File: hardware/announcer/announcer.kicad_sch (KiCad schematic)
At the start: 5 parts, among them Q1 S8050

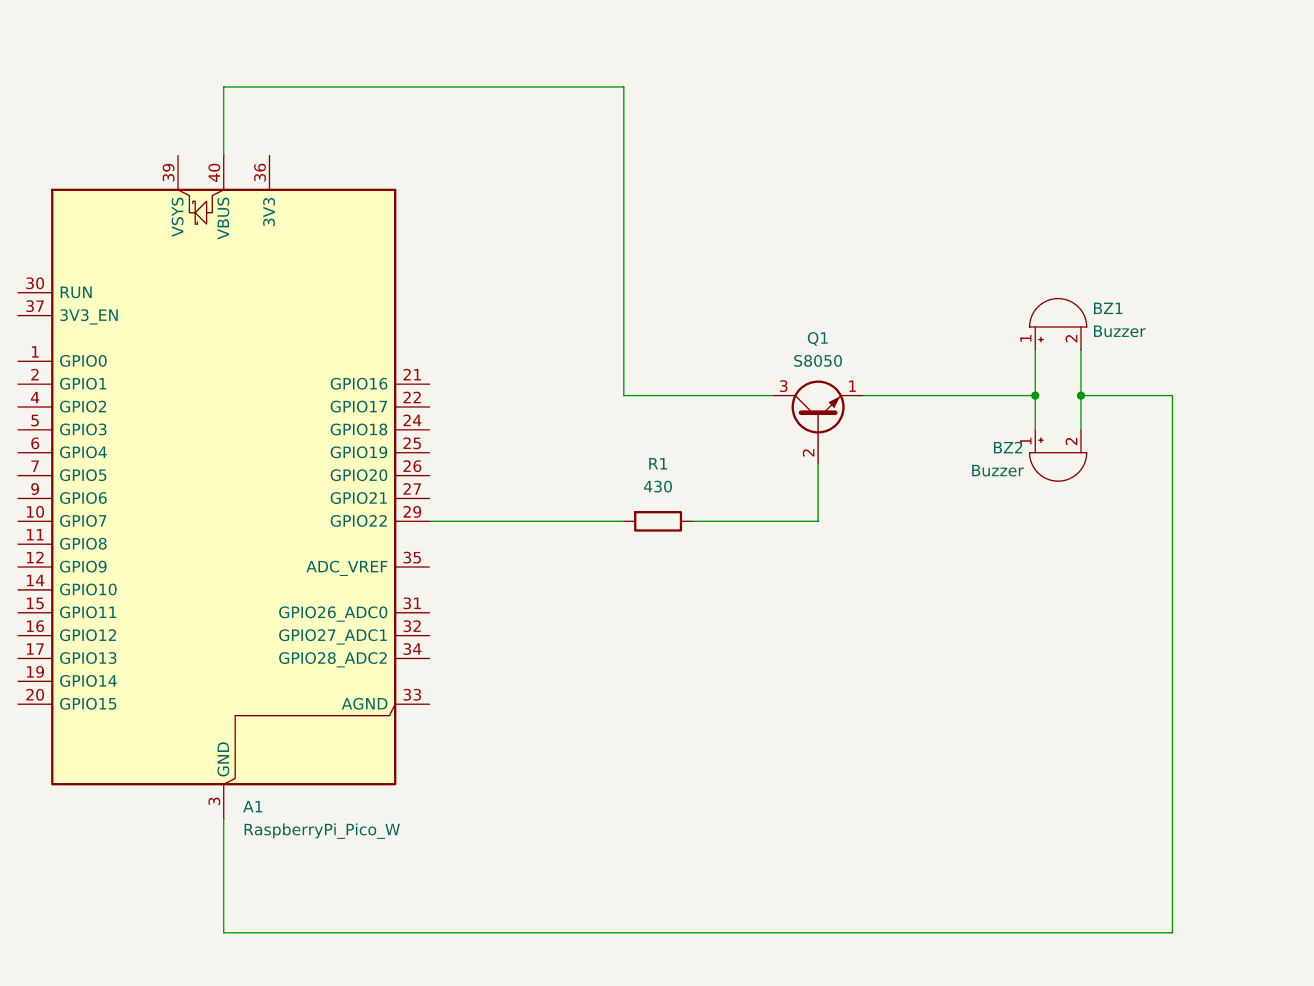
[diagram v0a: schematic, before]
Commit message: hardware announcer: updated schematic to include button and status LEDs
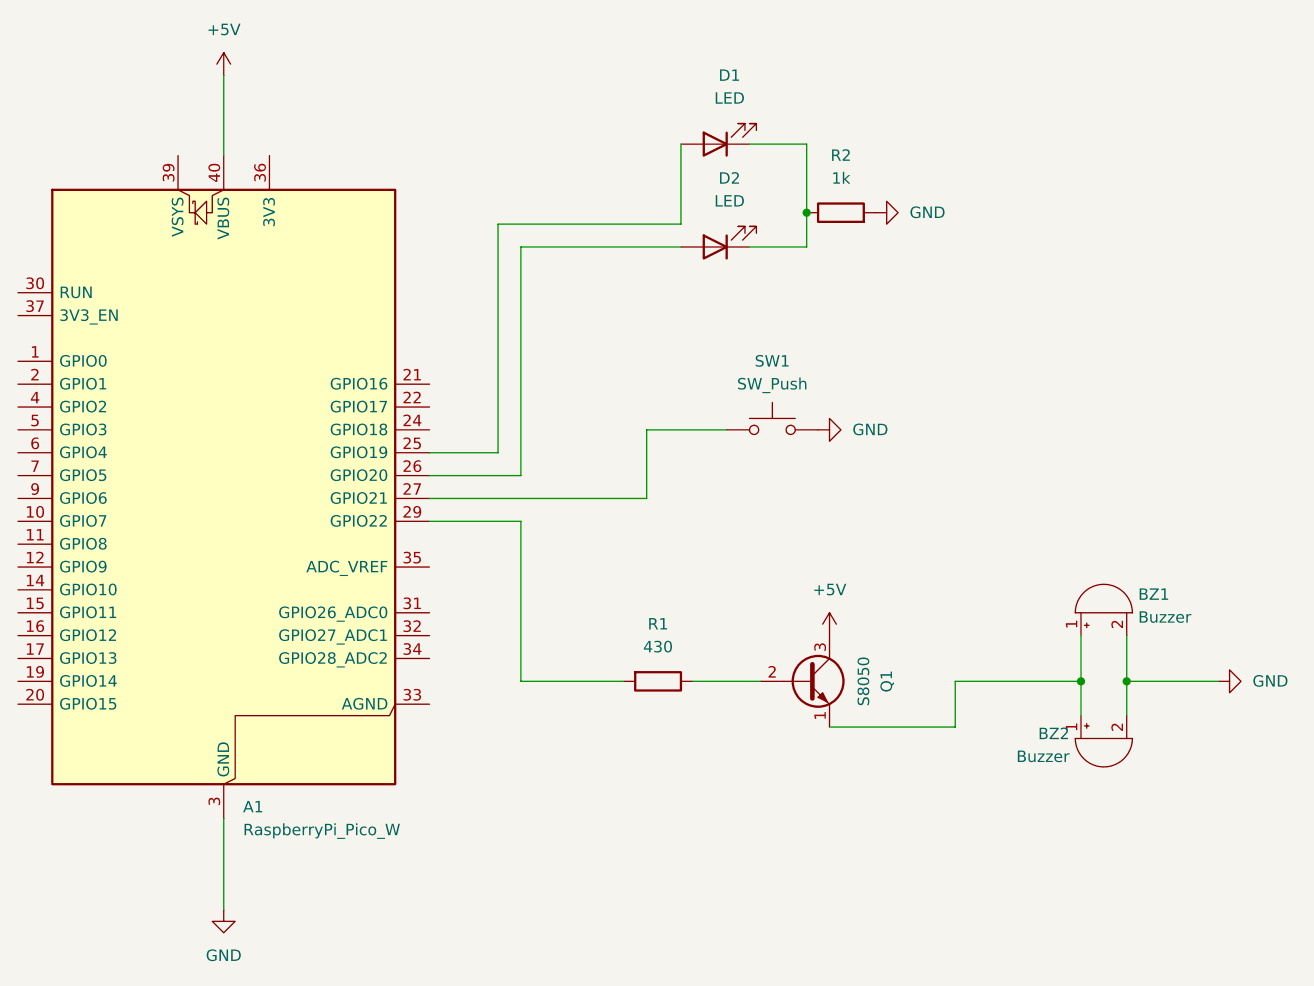
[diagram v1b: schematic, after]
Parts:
- added D1, D2: LED, symbol Device:LED
- added R2: 1k, symbol Device:R
- added SW1: SW_Push, symbol Switch:SW_Push
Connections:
- net GND: now reaches A1.13 (GND), A1.18 (GND), A1.23 (GND), A1.28 (GND), A1.3 (GND), A1.38 (GND), A1.8 (GND), BZ1.2 (-), BZ2.2 (-)
- net GND: now also R2.2, SW1.2
- net at A1.25 (GPIO19): now also D1.2 (A)
- net at A1.26 (GPIO20): now also D2.2 (A)
- net at A1.27 (GPIO21): now also SW1.1
- net +5V: now reaches A1.40 (VBUS), Q1.3 (C)
- new net: D1.1 (K), D2.1 (K), R2.1
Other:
- moved on the sheet: BZ1, BZ2, Q1, R1

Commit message: hardware announcer: update
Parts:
- BZ1, BZ2: footprint (none) -> JC-Library:Buzzer-TMB12A05
- D1, D2: footprint (none) -> LED_THT:LED_D2.0mm_W4.0mm_H2.8mm_FlatTop
- R1: footprint (none) -> Resistor_THT:R_Axial_DIN0207_L6.3mm_D2.5mm_P7.62mm_Horizontal
- R2: value 1k -> 1K; footprint (none) -> Resistor_THT:R_Axial_DIN0207_L6.3mm_D2.5mm_P7.62mm_Horizontal
- SW1: footprint (none) -> Button_Switch_THT:SW_PUSH_6mm_H8mm
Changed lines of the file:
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@@
 			)
 		)
-		(property "Footprint" ""
+		(property "Footprint" "Resistor_THT:R_Axial_DIN0207_L6.3mm_D2.5mm_P7.62mm_Horizontal"
 			(at 106.68 107.442 90)
 			(effects
@@
 			)
 		)
-		(property "Footprint" ""
+		(property "Footprint" "LED_THT:LED_D2.0mm_W4.0mm_H2.8mm_FlatTop"
 			(at 113.03 49.53 0)
 			(effects
@@
 		(exclude_from_sim no)
 		(in_bom yes)
-		(on_board yes)
+		(on_board no)
 		(dnp no)
 		(fields_autoplaced yes)
@@
 			)
 		)
-		(property "Value" "1k"
+		(property "Value" "1K"
 			(at 127 53.34 90)
 			(effects
@@
 			)
 		)
-		(property "Footprint" ""
+		(property "Footprint" "Resistor_THT:R_Axial_DIN0207_L6.3mm_D2.5mm_P7.62mm_Horizontal"
 			(at 127 58.928 90)
 			(effects
@@
 			)
 		)
-		(property "Footprint" ""
+		(property "Footprint" "Button_Switch_THT:SW_PUSH_6mm_H8mm"
 			(at 119.38 76.2 0)
 			(effects
@@
 			)
 		)
-		(property "Footprint" ""
+		(property "Footprint" "JC-Library:Buzzer-TMB12A05"
 			(at 153.67 102.235 90)
 			(effects
@@
 			)
 		)
-		(property "Footprint" ""
+		(property "Footprint" "JC-Library:Buzzer-TMB12A05"
 			(at 153.67 114.935 90)
 			(effects
@@
 			)
 		)
-		(property "Footprint" ""
+		(property "Footprint" "LED_THT:LED_D2.0mm_W4.0mm_H2.8mm_FlatTop"
 			(at 113.03 60.96 0)
 			(effects
